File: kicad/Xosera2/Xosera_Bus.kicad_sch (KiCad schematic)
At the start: 34 parts, among them IC1 74HCT245, IC2 74HCT245, IC3 ATF16V8BQL, IC4 GAL22V10, IC5 74HCT245, IC6 74LS74, J1 Conn_02x32_Odd_Even, J6 Conn_01x06_Male, Q1 2N3904

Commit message: Make a start on placement
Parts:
- removed IC1, IC2, IC5: 74HCT245, Package_DIP:DIP-20_W7.62mm_Socket_LongPads, symbol 74xx:74LS245
- removed R1, R2, R3, R4, R5, R6, R7, R8: R, rosco_m68k:R-0207_10, symbol Device:R
- added C45, C46, C47, C48: 100nF, Capacitor_SMD:C_0805_2012Metric, symbol Device:C_Small
- added U10, U9: TXB0108DQSR, Package_SO:TSSOP-20_4.4x6.5mm_P0.65mm, symbol Logic_LevelTranslator:TXB0108DQSR
- C1, C10, C11, C2, C3, C4, C5, C6, C9: footprint rosco_m68k:C2.5-3 -> Capacitor_SMD:C_0603_1608Metric
- IC6: value 74LS74 -> 74HCT74; footprint Package_DIP:DIP-14_W7.62mm_Socket_LongPads -> Package_SO:SOIC-14_3.9x8.7mm_P1.27mm
- Q1: footprint Package_TO_SOT_THT:TO-92_HandSolder -> Package_TO_SOT_SMD:SOT-23
- R9: footprint rosco_m68k:R-0207_10 -> Resistor_SMD:R_0603_1608Metric
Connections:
- net 68_D10: now also U9.18 (B3)
- net 68_D11: now also U9.17 (B4)
- net 68_D12: now also U9.14 (B5)
- net 68_D13: now also U9.13 (B6)
- net 68_D14: now also U9.12 (B7)
- net 68_D15: now also U9.11 (B8)
- net 68_D8: now also U9.20 (B1)
- net 68_D9: now also U9.19 (B2)
- net A1: now also U10.20 (B1)
- net A10: no longer IC3.5 (I5)
- net A11: no longer IC3.6 (I6)
- net A12: no longer IC3.7 (I7)
- net A13: no longer IC3.8 (I8)
- net A14: no longer IC3.9 (I9)
- net A17: no longer IC3.11 (I10/~{OE})
- net A2: now also U10.19 (B2)
- net A3: now also U10.18 (B3)
- net A4: now also U10.17 (B4)
- net A7: now also U10.14 (B5)
- net BUS_BYTESEL: now also U10.1 (A1)
- net BUS_DATA0: now also U9.1 (A1)
- net BUS_DATA1: now also U9.2 (A2)
- net BUS_DATA2: now also U9.3 (A3)
- net BUS_DATA3: now also U9.4 (A4)
- net BUS_DATA4: now also U9.7 (A5)
- net BUS_DATA5: now also U9.8 (A6)
- net BUS_DATA6: now also U9.9 (A7)
- net BUS_DATA7: now also U9.10 (A8)
- net BUS_REG_NUM0: now also U10.2 (A2)
- net BUS_REG_NUM1: now also U10.3 (A3)
- net BUS_REG_NUM2: now also U10.4 (A4)
- net BUS_REG_NUM3: now also U10.7 (A5)
- net BUS_R~{W}: now also U10.9 (A7)
- net FPGA_CS: now also U10.13 (B6), U9.6 (OE)
- net GND: now also C45.2, C46.2, C47.2, C48.2, U10.15 (GND), U10.6 (OE), U9.15 (GND)
- net RESET: now also U10.11 (B8)
- net RnW: now also U10.12 (B7)
- net ~{BUS_CS}: now also U10.8 (A6)
- net ~{JBUS_RESET}: now also U10.10 (A8)
- new net +3V3: C45.1, C47.1, U10.5 (VCCA), U9.5 (VCCA)
- new net +5VD: C46.1, C48.1, U10.16 (VCCB), U9.16 (VCCB)
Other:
- note removed: "All 470R"
- note removed: "FPGA_R is /RnW"
- moved on the sheet: C1, C10, C11, C2, C3, C4, C5, C6, C7, C8, C9, IC3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

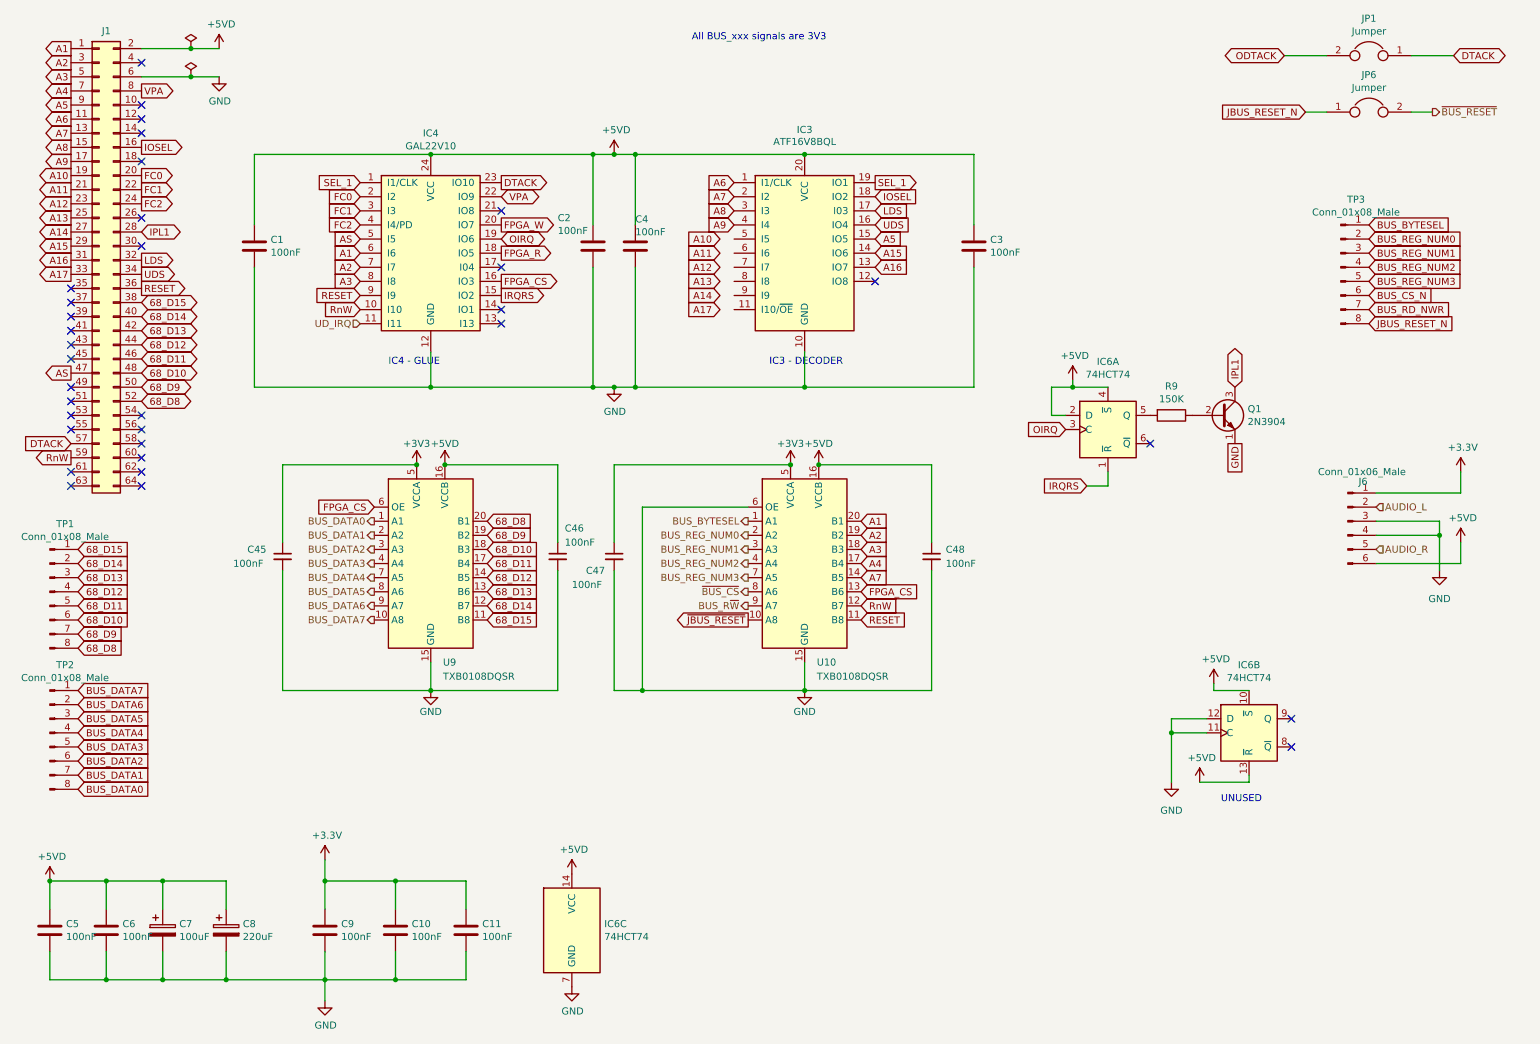
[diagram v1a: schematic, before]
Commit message: Replace all GALs with one 1504
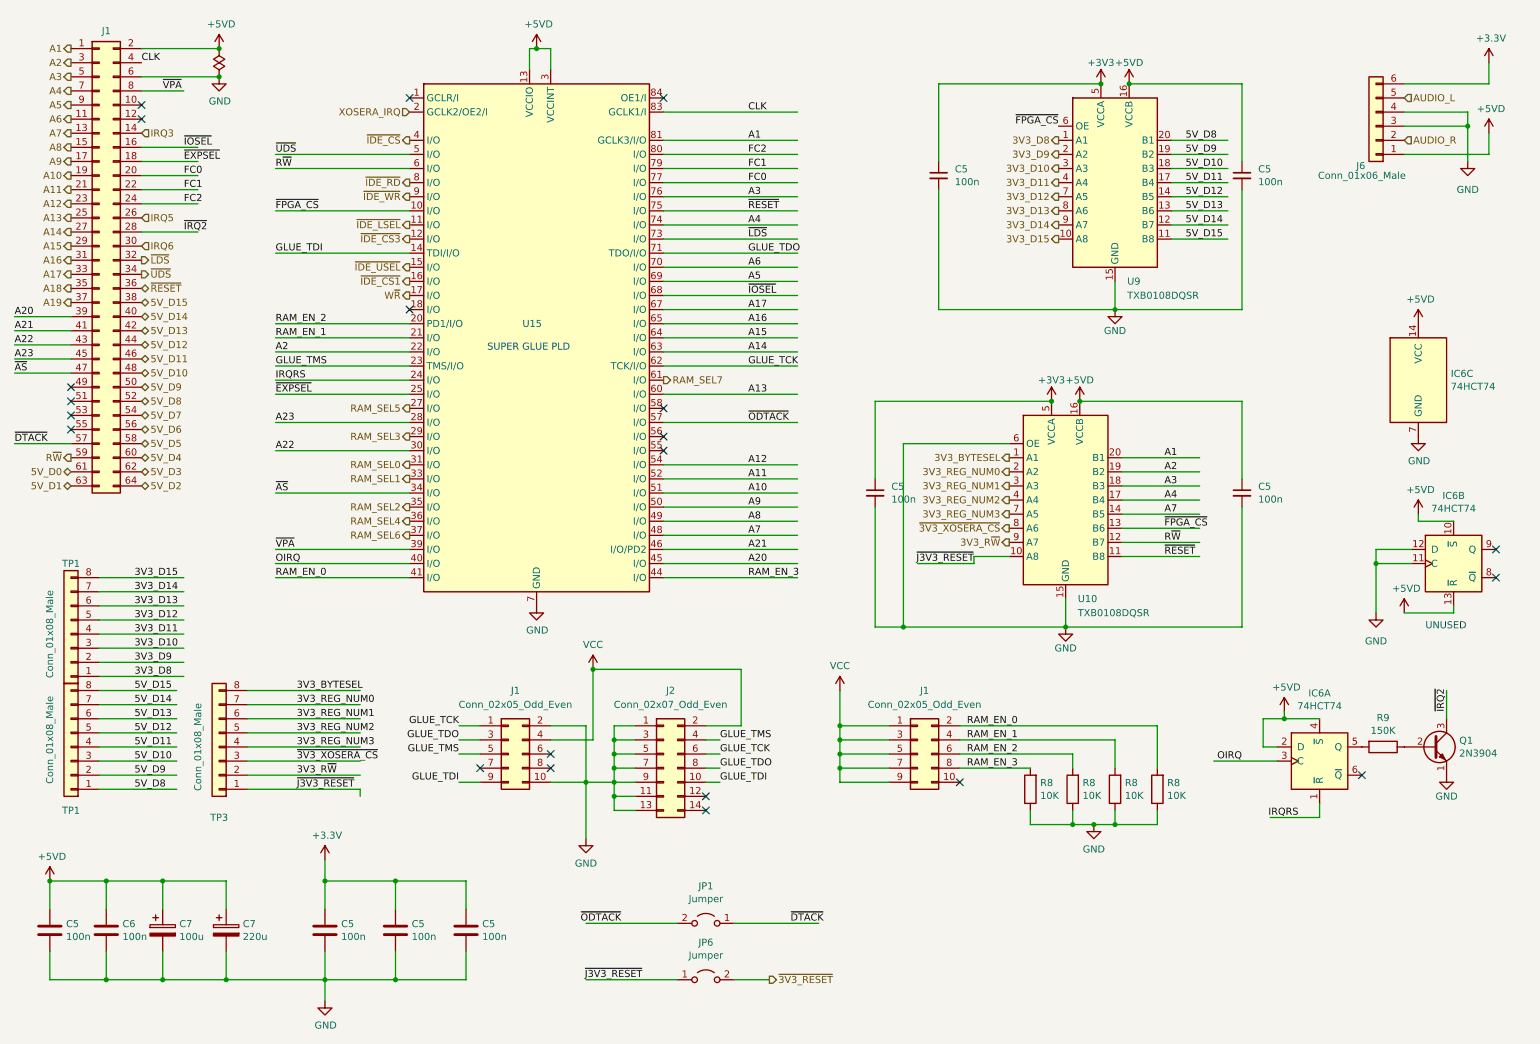
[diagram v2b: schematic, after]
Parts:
- removed C1, C10, C11, C2, C3, C4, C9: 100nF, Capacitor_SMD:C_0603_1608Metric, symbol Device:C
- removed C45, C46, C47, C48: 100nF, Capacitor_SMD:C_0805_2012Metric, symbol Device:C_Small
- removed C7: 100uF, Capacitor_THT:CP_Radial_D5.0mm_P2.50mm, symbol xosera-rescue:CP-Device
- removed C8: 220uF, Capacitor_THT:CP_Radial_D6.3mm_P2.50mm, symbol xosera-rescue:CP-Device
- removed IC3: ATF16V8BQL, Package_DIP:DIP-20_W7.62mm_Socket_LongPads, symbol Logic_Programmable:GAL16V8
- removed IC4: GAL22V10, Package_DIP:DIP-24_W7.62mm_LongPads, symbol rosco_m68k:GAL22V10
- removed TP2: Conn_01x08_Male, Connector_PinHeader_2.54mm:PinHeader_1x08_P2.54mm_Vertical, symbol xosera-rescue:Conn_01x08_Male-Connector
- added C5 (x4): 100n, Capacitor_SMD:C_0402_1005Metric, symbol Device:C_Small
- added C5 (x3): 100n, Capacitor_SMD:C_0402_1005Metric, symbol Device:C
- added C7: 100u, Capacitor_SMD:CP_Elec_6.3x5.4, symbol Device:C_Polarized
- added C7: 220u, Capacitor_SMD:CP_Elec_6.3x5.4, symbol Device:C_Polarized
- added J1 (x2): Conn_02x05_Odd_Even, Connector_IDC:IDC-Header_2x05_P2.54mm_Vertical, symbol Connector_Generic:Conn_02x05_Odd_Even
- added J2: Conn_02x07_Odd_Even, Connector_IDC:IDC-Header_2x07_P2.54mm_Vertical, symbol Connector_Generic:Conn_02x07_Odd_Even
- added R8 (x4): 10K, Resistor_SMD:R_0603_1608Metric, symbol Device:R
- added TP1: Conn_01x08_Male, Connector_PinHeader_2.54mm:PinHeader_1x08_P2.54mm_Vertical, symbol Connector_Generic:Conn_01x08
- added U15: ~, symbol CPLD_Microchip:ATF1504AS-PLCC84
- C5, C6: value 100nF -> 100n; footprint Capacitor_SMD:C_0603_1608Metric -> Capacitor_SMD:C_0402_1005Metric
- J6: symbol xosera-rescue:Conn_01x06_Male-Connector -> Connector_Generic:Conn_01x06
- JP1, JP6: symbol xosera-rescue:Jumper-Device -> Jumper:Jumper_2_Open
- TP1, TP3: symbol xosera-rescue:Conn_01x08_Male-Connector -> Connector_Generic:Conn_01x08
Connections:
- net BUS_R~{W} is gone; now on net 3V3_R~{W}: U10.9 (A7)
- net ~{BUS_CS} is gone; now on net ~{3V3_XOSERA_CS}: U10.8 (A6)
- net ~{JBUS_RESET} is gone; now on net ~{J3V3_RESET}: U10.10 (A8)
- net +3.3V: now also J6.6 (Pin_6), C5.1, C5.1, C5.1; no longer J6.1 (Pin_1)
- net +3V3: now also C5.1, C5.1
- net +5V: now also J6.1 (Pin_1), C7.1, C7.1, U15.13 (VCCIO), U15.26 (VCCIO), U15.3 (VCCINT), U15.38 (VCCIO), U15.43 (VCCINT), U15.53 (VCCIO), U15.66 (VCCIO), U15.78 (VCCIO); no longer J6.6 (Pin_6)
- net +5VD: now also C5.1, C5.1
- net A1: now also U15.81 (GCLK3/I/O)
- net A10: now also U15.51 (I/O)
- net A11: now also U15.52 (I/O)
- net A12: now also U15.54 (I/O)
- net A13: now also U15.60 (I/O)
- net A14: now also U15.63 (I/O)
- net A15: now also U15.64 (I/O)
- net A16: now also U15.65 (I/O)
- net A17: now also U15.67 (I/O)
- net A2: now also U15.22 (I/O)
- net A3: now also U15.76 (I/O)
- net A4: now also U15.74 (I/O)
- net A5: now also U15.69 (I/O)
- net A6: now also U15.70 (I/O)
- net A7: now also U15.48 (I/O)
- net A8: now also U15.49 (I/O)
- net A9: now also U15.50 (I/O)
- net AUDIO_L: now also J6.5 (Pin_5); no longer J6.2 (Pin_2)
- net AUDIO_R: now also J6.2 (Pin_2); no longer J6.5 (Pin_5)
- net FC0: now also U15.77 (I/O)
- net FC1: now also U15.79 (I/O)
- net FC2: now also U15.80 (I/O)
- net GND: now also C5.2, C5.2, C5.2, C5.2, C5.2, C5.2, C5.2, C7.2, C7.2, J1.10 (Pin_10), J1.2 (Pin_2), J2.1 (Pin_1), J2.11 (Pin_11), J2.13 (Pin_13), J2.3 (Pin_3), J2.5 (Pin_5), J2.7 (Pin_7), J2.9 (Pin_9), R8.1, R8.1, R8.1, R8.1, U15.19 (GND), U15.32 (GND), U15.42 (GND), U15.47 (GND), U15.59 (GND), U15.7 (GND), U15.72 (GND), U15.82 (GND)
- net IRQRS: now also U15.24 (I/O)
- net OIRQ: now also U15.40 (I/O)
- net IRQ3: now reaches J1.14 (Pin_14)
- net ~{EXPSEL}: now reaches J1.18 (Pin_18)
- net ~{EXPSEL}: now also U15.25 (I/O)
- net IRQ5: now reaches J1.26 (Pin_26)
- net IRQ6: now reaches J1.30 (Pin_30)
- net A18: now reaches J1.35 (Pin_35)
- net A19: now reaches J1.37 (Pin_37)
- net A20: now reaches J1.39 (Pin_39)
- net A20: now also U15.45 (I/O)
- net CLK: now reaches J1.4 (Pin_4)
- net CLK: now also U15.83 (GCLK1/I)
- net A21: now reaches J1.41 (Pin_41)
- net A21: now also U15.46 (I/O/PD2)
- net A22: now reaches J1.43 (Pin_43)
- net A22: now also U15.30 (I/O)
- net A23: now reaches J1.45 (Pin_45)
- net A23: now also U15.28 (I/O)
- net 5V_D7: now reaches J1.54 (Pin_54)
- net 5V_D6: now reaches J1.56 (Pin_56)
- net 5V_D5: now reaches J1.58 (Pin_58)
- net 5V_D4: now reaches J1.60 (Pin_60)
- net 5V_D0: now reaches J1.61 (Pin_61)
- net 5V_D3: now reaches J1.62 (Pin_62)
- net 5V_D1: now reaches J1.63 (Pin_63)
- net 5V_D2: now reaches J1.64 (Pin_64)
- net 68_D10 renamed 5V_D10
- net 5V_D10: now also TP1.3 (Pin_3); no longer TP1.6 (Pin_6)
- net 68_D11 renamed 5V_D11
- net 5V_D11: now also TP1.4 (Pin_4); no longer TP1.5 (Pin_5)
- net 68_D12 renamed 5V_D12
- net 5V_D12: now also TP1.5 (Pin_5); no longer TP1.4 (Pin_4)
- net 68_D13 renamed 5V_D13
- net 5V_D13: now also TP1.6 (Pin_6); no longer TP1.3 (Pin_3)
- net 68_D14 renamed 5V_D14
- net 5V_D14: now also TP1.7 (Pin_7); no longer TP1.2 (Pin_2)
- net 68_D15 renamed 5V_D15
- net 5V_D15: now also TP1.8 (Pin_8); no longer TP1.1 (Pin_1)
- net 68_D8 renamed 5V_D8
- net 5V_D8: now also TP1.1 (Pin_1); no longer TP1.8 (Pin_8)
- net 68_D9 renamed 5V_D9
- net 5V_D9: now also TP1.2 (Pin_2); no longer TP1.7 (Pin_7)
- net AS renamed ~{AS}
- net ~{AS}: now also U15.34 (I/O)
- net BUS_BYTESEL renamed 3V3_BYTESEL
- net 3V3_BYTESEL: now also TP3.8 (Pin_8); no longer TP3.1 (Pin_1)
- net BUS_CS_N renamed 3V3_REG_NUM1
- net 3V3_REG_NUM1: now also U10.3 (A3)
- net BUS_DATA0 renamed 3V3_D8
- net 3V3_D8: now also TP1.1 (Pin_1)
- net BUS_DATA1 renamed 3V3_D9
- net 3V3_D9: now also TP1.2 (Pin_2)
- net BUS_DATA2 renamed 3V3_D10
- net 3V3_D10: now also TP1.3 (Pin_3)
- net BUS_DATA3 renamed 3V3_D11
- net 3V3_D11: now also TP1.4 (Pin_4)
- net BUS_DATA4 renamed 3V3_D12
- net 3V3_D12: now also TP1.5 (Pin_5)
- net BUS_DATA5 renamed 3V3_D13
- net 3V3_D13: now also TP1.6 (Pin_6)
- net BUS_DATA6 renamed 3V3_D14
- net 3V3_D14: now also TP1.7 (Pin_7)
- net BUS_DATA7 renamed 3V3_D15
- net 3V3_D15: now also TP1.8 (Pin_8)
- net BUS_RD_NWR renamed 3V3_REG_NUM0
- net 3V3_REG_NUM0: now also U10.2 (A2)
- net BUS_REG_NUM0 renamed 3V3_R~{W}
- net 3V3_R~{W}: no longer U10.2 (A2)
- net BUS_REG_NUM1 renamed ~{3V3_XOSERA_CS}
- net ~{3V3_XOSERA_CS}: no longer U10.3 (A3)
- net BUS_REG_NUM2 renamed 3V3_REG_NUM2
- net 3V3_REG_NUM2: now also TP3.5 (Pin_5); no longer TP3.4 (Pin_4)
- net BUS_REG_NUM3 renamed 3V3_REG_NUM3
- net 3V3_REG_NUM3: now also TP3.4 (Pin_4); no longer TP3.5 (Pin_5)
- net DTACK renamed ~{DTACK}
- net FPGA_CS renamed ~{FPGA_CS}
- net ~{FPGA_CS}: now also U15.10 (I/O)
- net IOSEL renamed ~{IOSEL}
- net ~{IOSEL}: now also U15.68 (I/O)
- net IPL1 renamed ~{IRQ2}
- net JBUS_RESET_N renamed ~{J3V3_RESET}
- net ~{J3V3_RESET}: now also TP3.1 (Pin_1); no longer TP3.8 (Pin_8)
- net LDS renamed ~{LDS}
- net ~{LDS}: now also U15.73 (I/O)
- net ODTACK renamed ~{ODTACK}
- net ~{ODTACK}: now also U15.57 (I/O)
- net RESET renamed ~{RESET}
- net ~{RESET}: now also U15.75 (I/O)
- net RnW renamed R~{W}
- net R~{W}: now also U15.6 (I/O)
- net UDS renamed ~{UDS}
- net ~{UDS}: now also U15.5 (I/O)
- net VPA renamed ~{VPA}
- net ~{VPA}: now also U15.39 (I/O)
- net ~{BUS_RESET} renamed ~{3V3_RESET}
- new net GLUE_TCK: J1.1 (Pin_1), J2.6 (Pin_6), U15.62 (TCK/I/O)
- new net GLUE_TDI: J1.9 (Pin_9), J2.10 (Pin_10), U15.14 (TDI/I/O)
- new net GLUE_TDO: J1.3 (Pin_3), J2.8 (Pin_8), U15.71 (TDO/I/O)
- new net GLUE_TMS: J1.5 (Pin_5), J2.4 (Pin_4), U15.23 (TMS/I/O)
- new net RAM_EN_0: J1.2 (Pin_2), R8.2, U15.41 (I/O)
- new net RAM_EN_1: J1.4 (Pin_4), R8.2, U15.21 (I/O)
- new net RAM_EN_2: J1.6 (Pin_6), R8.2, U15.20 (PD1/I/O)
- new net RAM_EN_3: J1.8 (Pin_8), R8.2, U15.44 (I/O)
- new net RAM_SEL0: U15.31 (I/O)
- new net RAM_SEL1: U15.33 (I/O)
- new net RAM_SEL2: U15.35 (I/O)
- new net RAM_SEL3: U15.29 (I/O)
- new net RAM_SEL4: U15.36 (I/O)
- new net RAM_SEL5: U15.27 (I/O)
- new net RAM_SEL6: U15.37 (I/O)
- new net RAM_SEL7: U15.61 (I/O)
- new net VCC: J1.1 (Pin_1), J1.3 (Pin_3), J1.4 (Pin_4), J1.5 (Pin_5), J1.7 (Pin_7), J1.9 (Pin_9), J2.2 (Pin_2)
- new net W~{R}: U15.17 (I/O)
- new net XOSERA_IRQ: U15.2 (GCLK2/OE2/I)
- new net ~{IDE_CS1}: U15.16 (I/O)
- new net ~{IDE_CS3}: U15.12 (I/O)
- new net ~{IDE_CS}: U15.4 (I/O)
- new net ~{IDE_LSEL}: U15.11 (I/O)
- new net ~{IDE_RD}: U15.8 (I/O)
- new net ~{IDE_USEL}: U15.15 (I/O)
- new net ~{IDE_WR}: U15.9 (I/O)
- no-connect marks 33 -> 21
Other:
- note added: "SUPER GLUE PLD"
- note removed: "All BUS_xxx signals are 3V3"
- note removed: "IC3 - DECODER"
- note removed: "IC4 - GLUE"
- title: Xosera rosco_m68k daughterboard -> rosco_m68k Super Board
- moved on the sheet: IC6A, IC6B, IC6C, JP1, JP6, Q1, R9, U10, U9
